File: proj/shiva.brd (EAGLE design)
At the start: 68.8 x 43.2 mm, 22 parts, among them J1 DM3D-SFDM, J2 ADAFRUIT_OLED_13, SW1 TACTSWB3SL-10XXP, SW2 TACTSWB3SL-10XXP, SW3 TACTSWB3SL-10XXP, SW4 TACTSWB3SL-10XXP, SW5 TACTSWB3SL-10XXP, SW6 TACTSWB3SL-10XXP, SW7 TACTSWB3SL-10XXP, U1 MCP23008QFN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

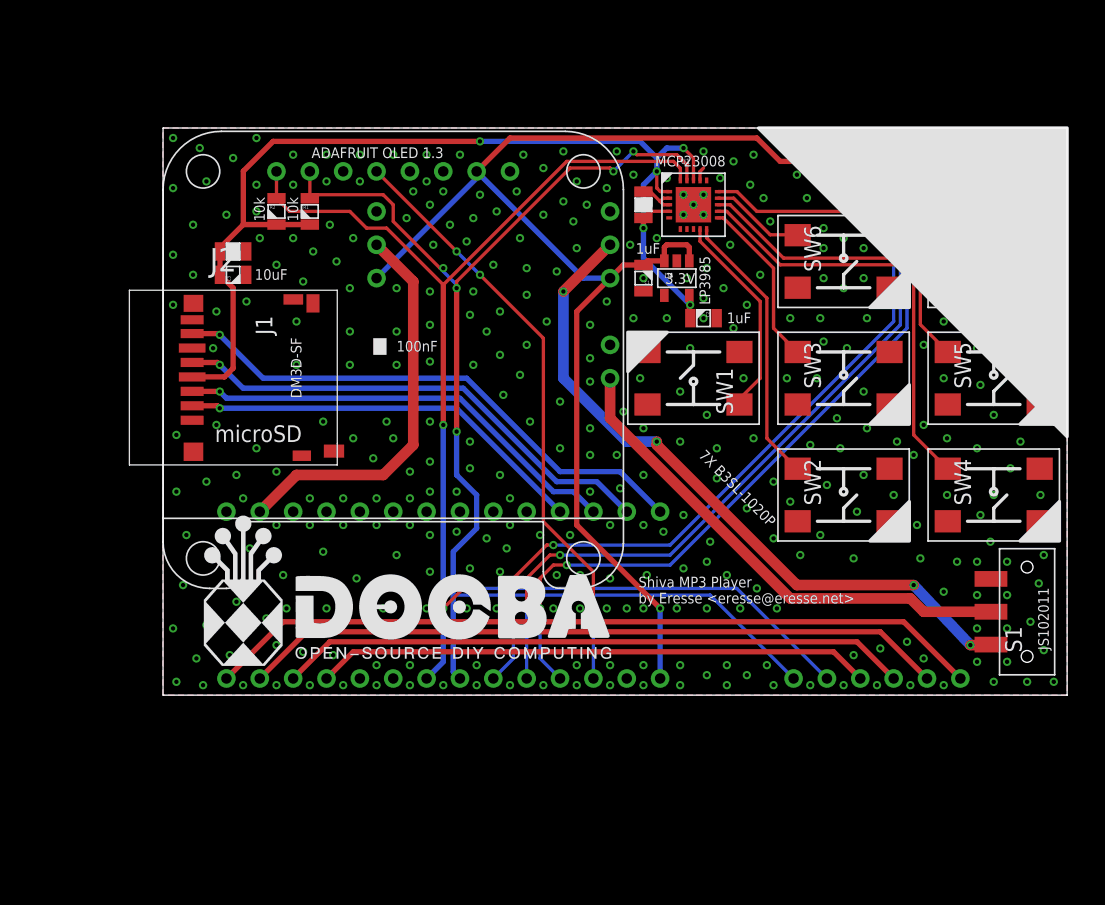
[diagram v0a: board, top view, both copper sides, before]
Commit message: Updated ioNode part in Eagle Library Integrated changes to ioNode part in Shiva board
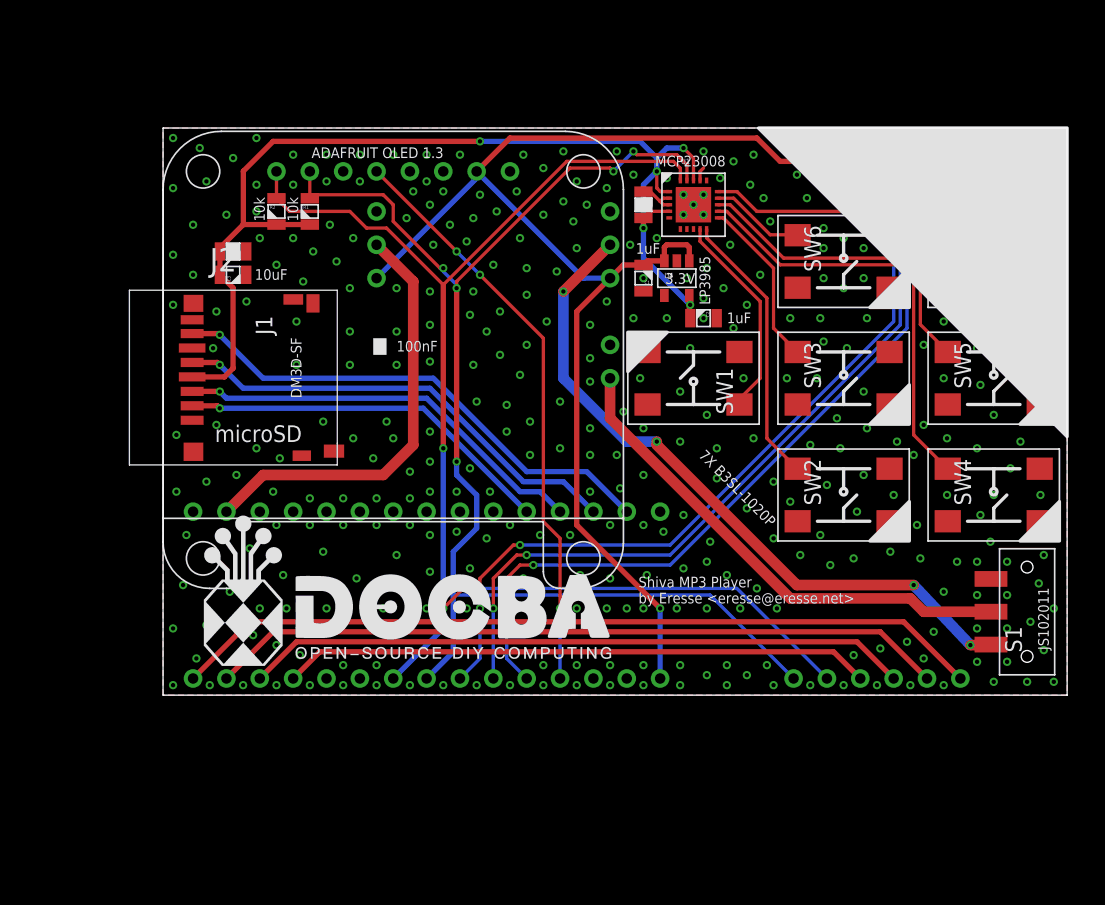
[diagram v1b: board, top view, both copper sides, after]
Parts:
- moved N1 2.54 mm to (49.5, 38.1)
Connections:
- net 5.5V: now also N1.16; no longer N1.15
- net AMP_CLK: now also N1.21; no longer N1.19
- net AMP_SHDN: now also N1.22; no longer N1.20
- net AMP_VUPDN: now also N1.20; no longer N1.18
- net GND: now also N1.15; no longer N1.16
- net I2C_SCL: now also N1.23; no longer N1.21
- net I2C_SDA: now also N1.24; no longer N1.22
- net MP3_DREQ: now also N1.29; no longer N1.27
- net MP3_RST: now also N1.30; no longer N1.28
- net MP3_SCKR: now also N1.27; no longer N1.25
- net MP3_SDI: now also N1.28; no longer N1.26
- net OLED_RST: now also N1.19; no longer N1.17
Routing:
- net MICROSD_SCK: track 37.8 -> 35.3 mm
- net AMP_CLK: track 58.6 -> 61.2 mm
- net MICROSD_MOSI: track 34.3 -> 31.8 mm
- net VUSB: track 30.2 -> 32.7 mm
- net MP3_SDI: track 48.0 -> 50.6 mm
- net MP3_SCKR: track 42.3 -> 44.9 mm
- net MP3_RST: track 59.5 -> 62.0 mm
- net MP3_DREQ: track 53.7 -> 56.3 mm
- net MICROSD_CS: track 31.3 -> 28.8 mm
- net AMP_VUPDN: track 59.7 -> 62.3 mm
- net AMP_SHDN: track 58.8 -> 61.3 mm
- net MICROSD_MISO: track 41.2 -> 38.7 mm
- net I2C_SDA: track 104.0 -> 105.0 mm
- net OLED_RST: track 45.4 -> 44.4 mm
- net I2C_SCL: track 101.1 -> 101.8 mm
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
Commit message: Routed stickie board Started designing Tako ethernet module Added ENC28J60 28QFN to Eagle Library
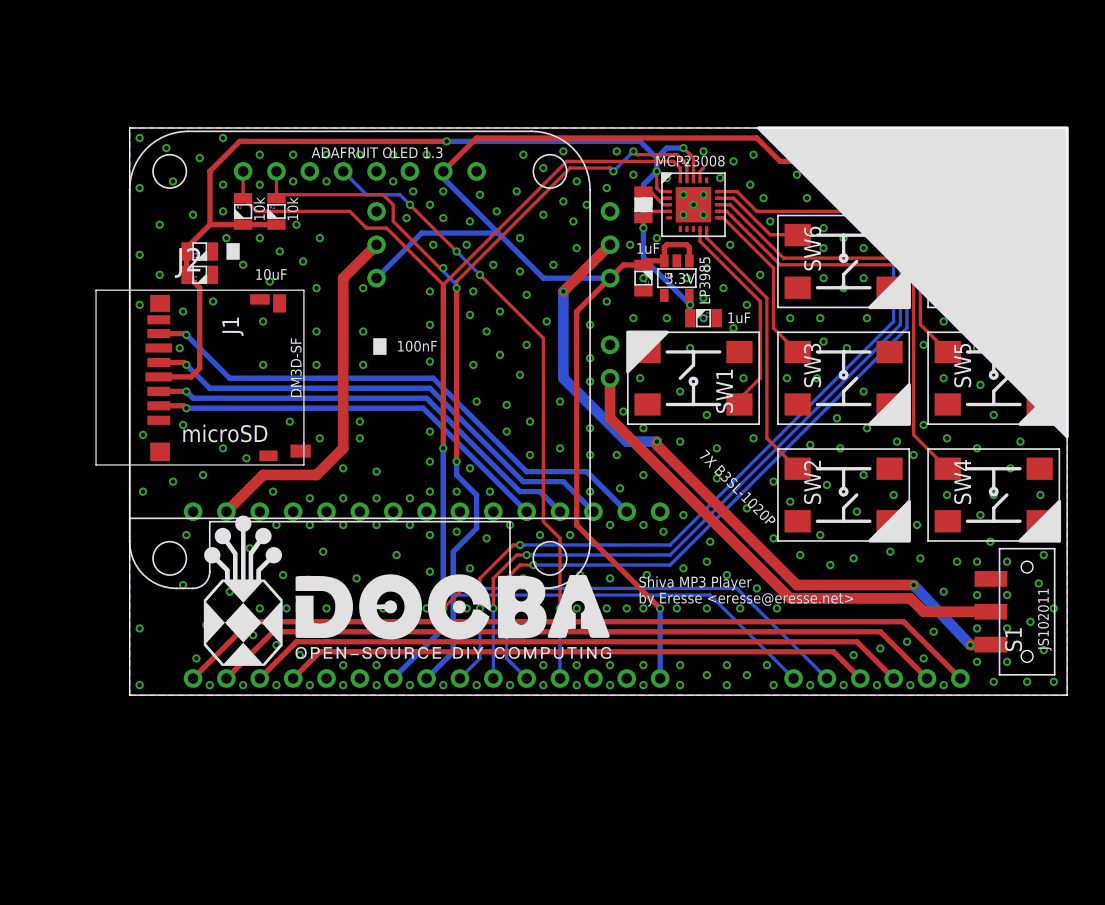
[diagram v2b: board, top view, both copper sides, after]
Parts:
- moved C3 2.54 mm to (33.5, 62.5)
- moved C4 2.54 mm to (33.5, 64.3)
- moved J1 2.54 mm to (31.8, 54.6)
- moved J2 2.54 mm to (45.7, 70.4)
- moved R1 2.54 mm to (39.4, 67.3)
- moved R2 2.54 mm to (36.8, 67.3)
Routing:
- net VUSB: track 32.7 -> 27.4 mm
- net 5.5V: track 96.8 -> 101.5 mm
- net MICROSD_SCK: track 35.3 -> 37.8 mm
- net 3.3V: track 83.6 -> 86.1 mm
- net OLED_RST: track 44.4 -> 46.9 mm, vias 3 -> 4
- net MICROSD_MISO: track 38.7 -> 41.2 mm
- net MICROSD_CS: track 28.8 -> 31.3 mm
- net MICROSD_MOSI: track 31.8 -> 34.3 mm
- net I2C_SDA: track 105.0 -> 107.5 mm
- net I2C_SCL: track 101.8 -> 104.3 mm
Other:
- board size 68.8 x 43.2 mm -> 71.4 x 43.2 mm

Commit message: Started re-designing Shiva MP3 schematic & board for hardware SPI Also, made it smaller :) @open #7
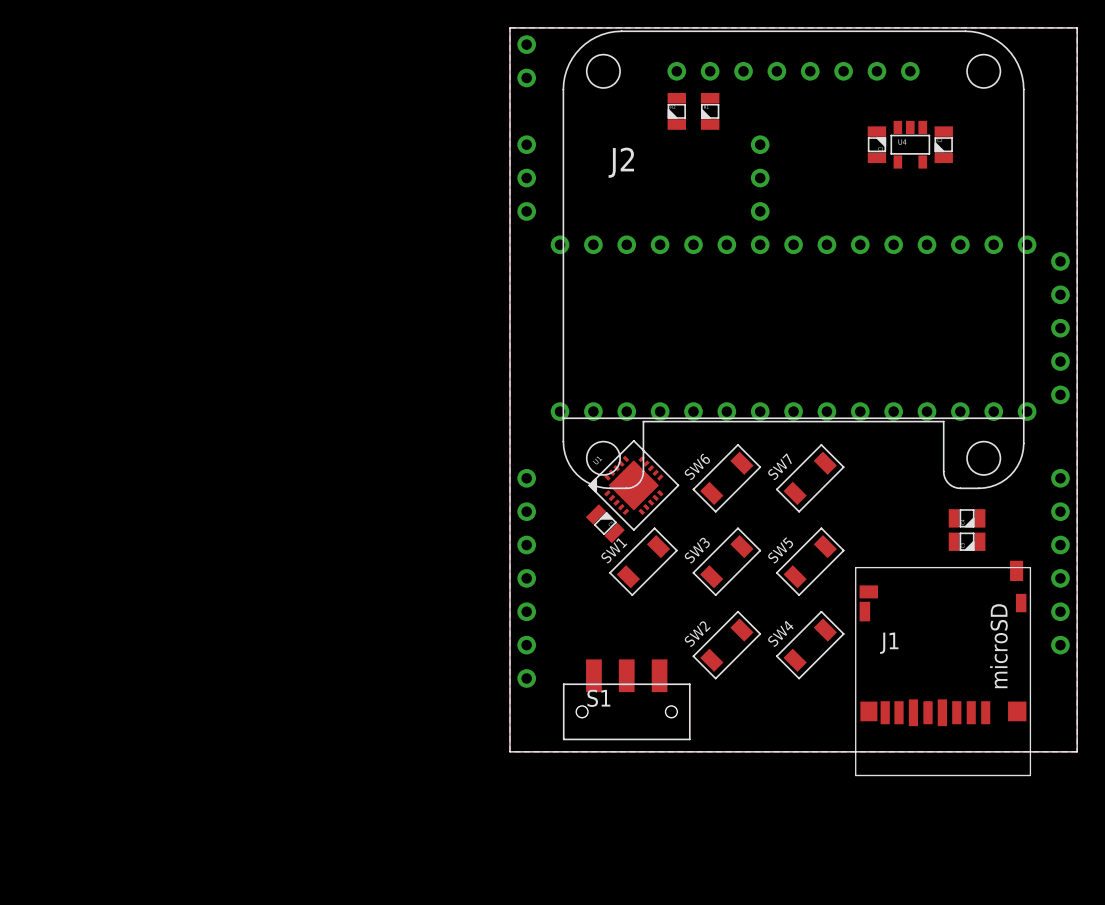
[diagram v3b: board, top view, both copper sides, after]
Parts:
- SW1, SW2, SW3, SW4, SW5, SW6, SW7: value TACTSWB3SL-10XXP -> TACTSW_2CK_KXT3; device dooba:B3SL-10XXP -> dooba:CK_KXT3
- moved J1 63.2 mm to (90.2, 30.5), turned to 0 degrees
- moved C3 61.9 mm to (91.9, 42.2)
- moved C4 61.9 mm to (91.9, 43.9)
- moved N1 34.5 mm to (77.5, 58.4)
- moved R1 33.9 mm to (72.4, 74.9)
- moved R2 33.9 mm to (69.8, 74.9)
- moved J2 33.9 mm to (78.7, 78.0)
- moved S1 31.4 mm to (66.0, 29.2), turned to 0 degrees
- moved C5 24.5 mm to (64.4, 43.5), turned to 135 degrees
- moved C2 22.6 mm to (90.2, 72.4), turned to 270 degrees
- moved U1 21.8 mm to (66.6, 46.5), turned to 45 degrees
- moved SW7 21.6 mm to (80.0, 47.0), turned to 45 degrees
- moved C1 20.5 mm to (85.1, 72.4)
- moved U4 20.5 mm to (87.6, 72.4)
- moved SW5 19.8 mm to (80.0, 40.6), turned to 45 degrees
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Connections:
- removed net MICROSD_MISO: J1.DAT0/DO, N1.14
- removed net MICROSD_MOSI: J1.CMD/DI, N1.12
- removed net MICROSD_SCK: J1.CLK/SCK, N1.13
- removed net MP3_SCKR: N1.27, U2.10
- removed net MP3_SDI: N1.28, U2.9
- new net MP3_BIT_EN: U2.7
- new net SPI_MISO: J1.DAT0/DO, N1.32
- new net SPI_MOSI: J1.CMD/DI, N1.31, U2.10
- new net SPI_SCK: J1.CLK/SCK, N1.33, U2.11
- net GND: now also N1.35, SW1.P$2, SW2.P$2, SW3.P$2, SW4.P$2, SW5.P$2, SW6.P$2, SW7.P$2; no longer SW1.3, SW2.3, SW3.3, SW4.3, SW5.3, SW6.3, SW7.3
- net I2C_SCL: now also U2.13; no longer U2.12
- net I2C_SDA: now also U2.12; no longer U2.11
- net MP3_DREQ: now also U2.9; no longer U2.8
- net MP3_RST: now also U2.8; no longer U2.7
- net N$1: now also SW1.P$1; no longer SW1.1
- net N$2: now also SW2.P$1; no longer SW2.1
- net N$3: now also SW3.P$1; no longer SW3.1
- net N$4: now also SW4.P$1; no longer SW4.1
- net N$5: now also SW5.P$1; no longer SW5.1
- net N$6: now also SW6.P$1; no longer SW6.1
- net N$7: now also SW7.P$1; no longer SW7.1
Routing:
- net I2C_SDA: track 107.5 -> 0.00 mm, vias 3 -> 0
- net I2C_SCL: track 104.3 -> 0.00 mm, vias 5 -> 0
- net 5.5V: track 101.5 -> 0.00 mm, vias 1 -> 0
- net 3.3V: track 86.1 -> 0.00 mm, vias 5 -> 0
- net AMP_VUPDN: track 62.3 -> 0.00 mm, vias 2 -> 0
- net MP3_RST: track 62.0 -> 0.00 mm
- net AMP_SHDN: track 61.3 -> 0.00 mm, vias 2 -> 0
- net AMP_CLK: track 61.2 -> 0.00 mm, vias 2 -> 0
- net MP3_DREQ: track 56.3 -> 0.00 mm
- net N$11: track 52.8 -> 0.00 mm, vias 4 -> 0
- net MP3_SDI: track 50.6 -> 0.00 mm
- net OLED_RST: track 46.9 -> 0.00 mm, vias 4 -> 0
- net MP3_SCKR: track 44.9 -> 0.00 mm
- net MICROSD_MISO: track 41.2 -> 0.00 mm, vias 1 -> 0
- net VBAT: track 38.2 -> 0.00 mm
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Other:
- board size 71.4 x 43.2 mm -> 43.2 x 55.1 mm
- board text removed: "100nF"
- board text removed: "10k"
- board text removed: "10uF"
- board text removed: "1uF"
- board text removed: "3.3V"
- board text removed: "7X B3SL-1020P"
- board text removed: "ADAFRUIT OLED 1.3"
- board text removed: "Aecho"
- board text removed: "DM3D-SF"
- board text removed: "JS102011"
- board text removed: "LP3985"
- board text removed: "MCP23008"
- board text removed: "Nomad"
- board text removed: "Shiva MP3 Player by Eresse <eresse@eresse.net>"
- board text removed: "ioNode"

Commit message: Completed new Shiva board using SPI for MicroSD and Aecho Improved some QFN parts in the Eagle Library Added ref layer to Nomad for ZFPCBA @close #7
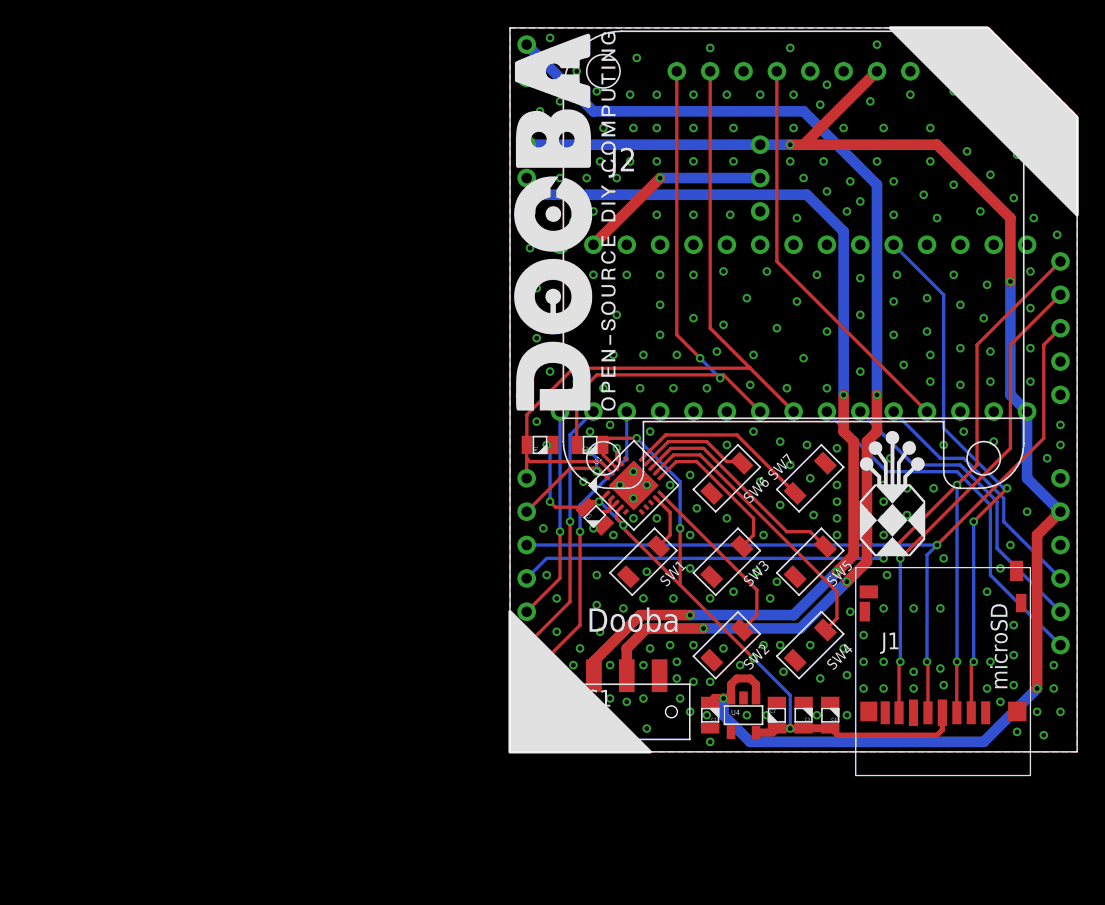
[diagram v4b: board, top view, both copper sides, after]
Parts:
- moved C1 45.3 mm to (72.4, 29.0)
- moved C2 45.3 mm to (77.5, 29.0)
- moved U4 45.3 mm to (74.9, 29.0)
- moved R1 28.5 mm to (59.4, 49.5), turned to 0 degrees
- moved R2 26.2 mm to (63.2, 49.5), turned to 0 degrees
- moved C4 18.2 mm to (81.5, 29.0), turned to 90 degrees
- moved C3 18.1 mm to (79.5, 29.0), turned to 90 degrees
- moved C5 0.98 mm to (63.6, 44.1), turned to 315 degrees
- turned SW1 to 225 degrees
- turned SW2 to 225 degrees
- turned SW3 to 225 degrees
- turned SW4 to 225 degrees
- turned SW5 to 225 degrees
- turned SW6 to 225 degrees
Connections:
- net AMP_SHDN: now also N1.20; no longer N1.22
- net AMP_VUPDN: now also N1.22; no longer N1.20
- net MP3_BIT_EN: now also N1.28
- net MP3_DREQ: now also N1.30; no longer N1.29
- net MP3_RST: now also N1.29; no longer N1.30
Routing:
- net 5.5V: track 0.00 -> 119.0 mm, vias 0 -> 4
- net VBAT: track 0.00 -> 83.2 mm, vias 0 -> 3
- net N$11: track 0.00 -> 75.0 mm, vias 0 -> 3
- net SPI_MOSI: track 0.00 -> 73.3 mm, vias 0 -> 3
- net 3.3V: track 0.00 -> 69.7 mm, vias 0 -> 8
- net SPI_SCK: track 0.00 -> 64.8 mm, vias 0 -> 2
- net I2C_SCL: track 0.00 -> 58.8 mm
- net I2C_SDA: track 0.00 -> 55.8 mm, vias 0 -> 4
- net MICROSD_CS: track 0.00 -> 40.5 mm, vias 0 -> 3
- net SPI_MISO: track 0.00 -> 36.9 mm, vias 0 -> 2
- net OLED_RST: track 0.00 -> 30.6 mm
- net AMP_VUPDN: track 0.00 -> 28.3 mm
- net AMP_CLK: track 0.00 -> 23.6 mm
- net MP3_BIT_EN: track 0.00 -> 23.5 mm, vias 0 -> 1
- net N$4: track 0.00 -> 22.0 mm
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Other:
- outline, holes or cut-outs redrawn
- board text added: "Dooba"

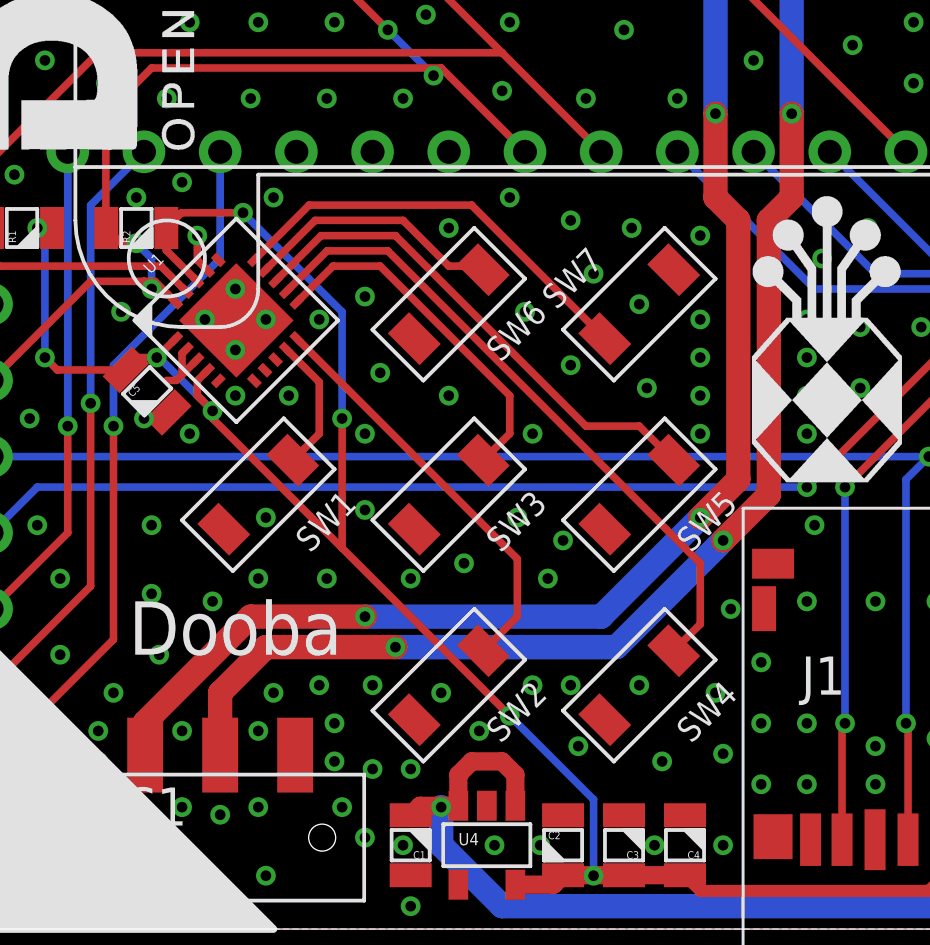
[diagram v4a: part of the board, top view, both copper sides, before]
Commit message: Fixed Buttons on Shiva MP3 board (buttons were too close to OLED)
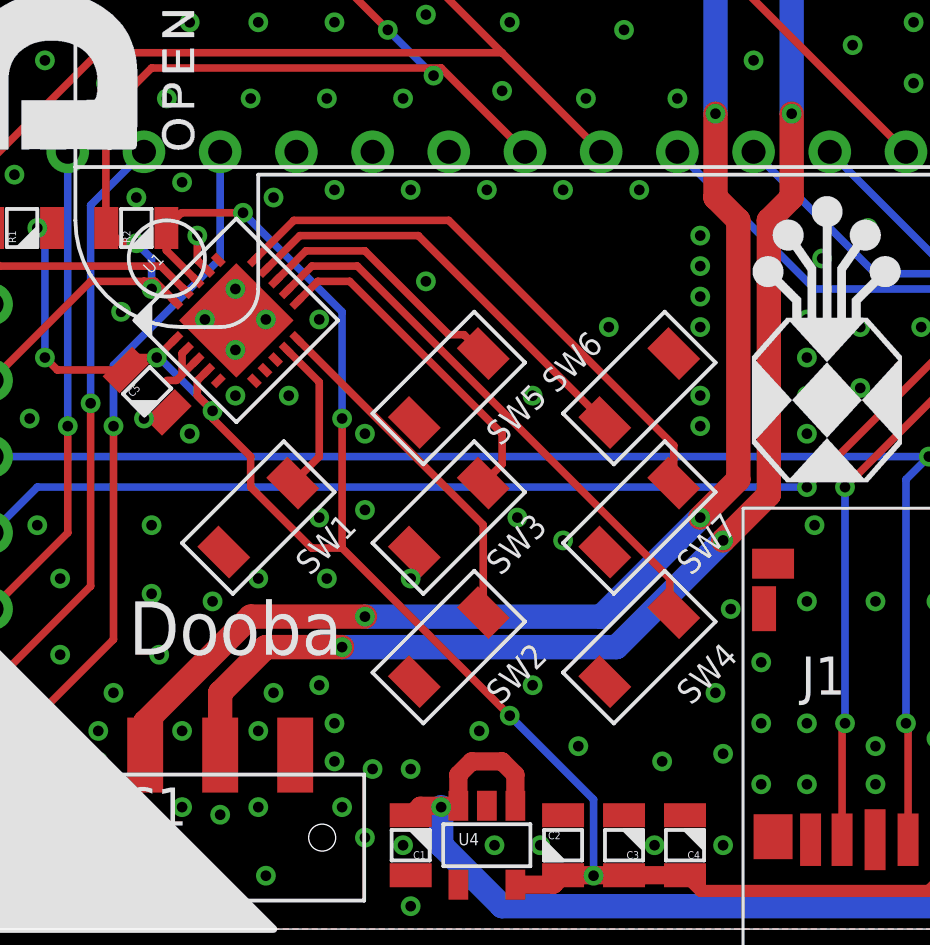
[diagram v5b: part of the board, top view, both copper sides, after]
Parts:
- moved SW5 7.28 mm to (73.7, 44.2)
- moved SW7 7.11 mm to (80.0, 39.9), turned to 225 degrees
- moved SW6 6.94 mm to (80.0, 44.2), turned to 45 degrees
- moved SW2 1.27 mm to (73.7, 35.6)
- moved SW4 1.27 mm to (80.0, 35.6)
- moved SW1 0.76 mm to (67.3, 39.9)
- moved SW3 0.76 mm to (73.7, 39.9)
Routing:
- net N$5: track 17.0 -> 8.76 mm
- net N$6: track 8.65 -> 14.4 mm
- net N$7: track 14.3 -> 18.9 mm
- net N$4: track 22.0 -> 18.6 mm
- net N$2: track 13.9 -> 11.7 mm
- net N$1: track 4.53 -> 5.29 mm
- net N$3: track 11.9 -> 11.1 mm
- net 3.3V: track 69.7 -> 70.3 mm
- net GND: vias 272 -> 262
